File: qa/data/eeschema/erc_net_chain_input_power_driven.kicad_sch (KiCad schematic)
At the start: 5 parts

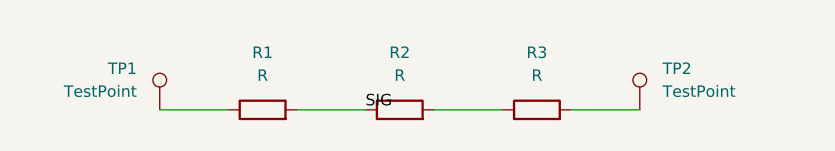
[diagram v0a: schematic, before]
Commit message: Fully rename signals to netchain
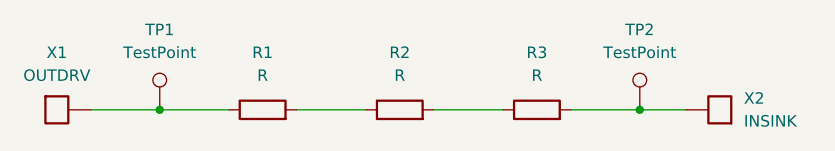
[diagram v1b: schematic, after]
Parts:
- added X1: OUTDRV, symbol Custom:OUTDRV
- added X2: INSINK, symbol Custom:OUTDRV
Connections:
- net at R1.1, TP1.1: now also X1.1
- net at R3.2, TP2.1: now also X2.1
- net SIG: no longer names the net of R1.2, R2.1
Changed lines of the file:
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@@
 	(generator_version "9.99")
 	(paper "A4")
+	(junction
+		(at 90.17 87.63)
+		(diameter 0)
+		(color 0 0 0 0)
+	)
+	(junction
+		(at 143.51 87.63)
+		(diameter 0)
+		(color 0 0 0 0)
+	)
+	(wire
+		(pts
+			(xy 82.55 87.63) (xy 90.17 87.63)
+		)
+		(stroke
+			(width 0)
+			(type default)
+		)
+	)
+	(wire
+		(pts
+			(xy 143.51 87.63) (xy 148.59 87.63)
+		)
+		(stroke
+			(width 0)
+			(type default)
+		)
+	)
 	(wire
 		(pts
@@
 		)
 	)
-	(label "SIG"
-		(at 113.03 87.63 0)
-		(effects
-			(font
-				(size 1.27 1.27)
-			)
-			(justify bottom)
-		)
-	)
 	(symbol
 		(lib_id "Connector:TestPoint")
@@
 		(on_board yes)
 		(dnp no)
+		(fields_autoplaced yes)
 		(property "Reference" "TP1"
-			(at 87.63 83.0579 0)
-			(effects
-				(font
-					(size 1.27 1.27)
-				)
-				(justify right)
+			(at 90.17 78.74 0)
+			(effects
+				(font
+					(size 1.27 1.27)
+				)
 			)
 		)
 		(property "Value" "TestPoint"
-			(at 87.63 85.5979 0)
-			(effects
-				(font
-					(size 1.27 1.27)
-				)
-				(justify right)
+			(at 90.17 81.28 0)
+			(effects
+				(font
+					(size 1.27 1.27)
+				)
 			)
 		)
@@
 		)
 		(instances
-			(project "signals_four_nets_labeled"
-				(path "/4daf6ccb-9a37-44a0-bb66-d9bcd0e8fa25"
+			(project "erc_signal_pin_to_pin"
+				(path "/4b4054a5-3d16-4add-856b-8e9bdcb8c9d3"
 					(reference "TP1")
 					(unit 1)
@@
 		)
 		(instances
-			(project "signals_four_nets_labeled"
-				(path "/4daf6ccb-9a37-44a0-bb66-d9bcd0e8fa25"
+			(project "erc_signal_pin_to_pin"
+				(path "/4b4054a5-3d16-4add-856b-8e9bdcb8c9d3"
 					(reference "R2")
+					(unit 1)
+				)
+			)
+		)
+	)
+	(symbol
+		(lib_name "OUTDRV_1")
+		(lib_id "Custom:OUTDRV")
+		(at 78.74 87.63 0)
+		(unit 1)
+		(body_style 1)
+		(exclude_from_sim no)
+		(in_bom yes)
+		(on_board yes)
+		(dnp no)
+		(fields_autoplaced yes)
+		(property "Reference" "X1"
+			(at 78.74 81.28 0)
+			(effects
+				(font
+					(size 1.27 1.27)
+				)
+			)
+		)
+		(property "Value" "OUTDRV"
+			(at 78.74 83.82 0)
+			(effects
+				(font
+					(size 1.27 1.27)
+				)
+			)
+		)
+		(property "Footprint" ""
+			(at 78.74 87.63 0)
+			(effects
+				(font
+					(size 1.27 1.27)
+				)
+			)
+		)
+		(property "Datasheet" ""
+			(at 78.74 87.63 0)
+			(effects
+				(font
+					(size 1.27 1.27)
+				)
+			)
+		)
+		(property "Description" ""
+			(at 78.74 87.63 0)
+			(effects
+				(font
+					(size 1.27 1.27)
+				)
+			)
+		)
+		(pin "1"
+		)
+		(instances
+			(project "erc_signal_pin_to_pin"
+				(path "/4b4054a5-3d16-4add-856b-8e9bdcb8c9d3"
+					(reference "X1")
 					(unit 1)
 				)
@@
 		)
 		(instances
-			(project "signals_four_nets_labeled"
-				(path "/4daf6ccb-9a37-44a0-bb66-d9bcd0e8fa25"
+			(project "erc_signal_pin_to_pin"
+				(path "/4b4054a5-3d16-4add-856b-8e9bdcb8c9d3"
 					(reference "R1")
+					(unit 1)
+				)
+			)
+		)
+	)
+	(symbol
+		(lib_id "Custom:OUTDRV")
+		(at 152.4 87.63 180)
+		(unit 1)
+		(body_style 1)
+		(exclude_from_sim no)
+		(in_bom yes)
+		(on_board yes)
+		(dnp no)
+		(fields_autoplaced yes)
+		(property "Reference" "X2"
+			(at 155.07 86.3599 0)
+			(effects
+				(font
+					(size 1.27 1.27)
+				)
+				(justify right)
+			)
+		)
+		(property "Value" "INSINK"
+			(at 155.07 88.8999 0)
+			(effects
+				(font
+					(size 1.27 1.27)
+				)
+				(justify right)
+			)
+		)
+		(property "Footprint" ""
+			(at 152.4 87.63 0)
+			(effects
+				(font
+					(size 1.27 1.27)
+				)
+			)
+		)
+		(property "Datasheet" ""
+			(at 152.4 87.63 0)
+			(effects
+				(font
+					(size 1.27 1.27)
+				)
+			)
+		)
+		(property "Description" ""
+			(at 152.4 87.63 0)
+			(effects
+				(font
+					(size 1.27 1.27)
+				)
+			)
+		)
+		(pin "1"
+		)
+		(instances
+			(project "erc_signal_pin_to_pin"
+				(path "/4b4054a5-3d16-4add-856b-8e9bdcb8c9d3"
+					(reference "X2")
 					(unit 1)
 				)
@@
 		)
 		(instances
-			(project "signals_four_nets_labeled"
-				(path "/4daf6ccb-9a37-44a0-bb66-d9bcd0e8fa25"
+			(project "erc_signal_pin_to_pin"
+				(path "/4b4054a5-3d16-4add-856b-8e9bdcb8c9d3"
 					(reference "R3")
 					(unit 1)
@@
 		(fields_autoplaced yes)
 		(property "Reference" "TP2"
-			(at 146.05 83.0579 0)
-			(effects
-				(font
-					(size 1.27 1.27)
-				)
-				(justify left)
+			(at 143.51 78.74 0)
+			(effects
+				(font
+					(size 1.27 1.27)
+				)
 			)
 		)
 		(property "Value" "TestPoint"
-			(at 146.05 85.5979 0)
-			(effects
-				(font
-					(size 1.27 1.27)
-				)
-				(justify left)
+			(at 143.51 81.28 0)
+			(effects
+				(font
+					(size 1.27 1.27)
+				)
 			)
 		)
@@
 		)
 		(instances
-			(project "signals_four_nets_labeled"
-				(path "/4daf6ccb-9a37-44a0-bb66-d9bcd0e8fa25"
+			(project "erc_signal_pin_to_pin"
+				(path "/4b4054a5-3d16-4add-856b-8e9bdcb8c9d3"
 					(reference "TP2")
 					(unit 1)
@@
 		)
 	)
-	(signal "SIG"
+	(net_chain "Signal1"
 	)
 	(sheet_instances
